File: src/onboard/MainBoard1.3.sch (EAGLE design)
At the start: 82 parts, among them IC1 MIC29310-5.0BT, IC3 A5975D, U1 ADAFRUIT_BMP280_BAROMETER

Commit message: Added gnd test point
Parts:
- added GND: PTR1B1,27, testpad:PTR1B1,27
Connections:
- net GND: now also GND.TP
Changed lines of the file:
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@@
 <part name="C4" library="capacitor-wima" library_urn="urn:adsk.eagle:library:116" deviceset="C" device="2,5-3" package3d_urn="urn:adsk.eagle:package:5436/1" value="10uF"/>
 <part name="SJ1" library="jumper" library_urn="urn:adsk.eagle:library:252" deviceset="SJ" device="" package3d_urn="urn:adsk.eagle:package:15471/1"/>
+<part name="GND" library="testpad" library_urn="urn:adsk.eagle:library:385" deviceset="PTR1" device="B1,27" package3d_urn="urn:adsk.eagle:package:27944/2"/>
 </parts>
 <sheets>
@@
 <attribute name="TP_SIGNAL_NAME" x="10.16" y="69.85" size="1.778" layer="97" rot="R270"/>
 </instance>
+<instance part="GND" gate="G$1" x="12.7" y="45.72" smashed="yes" rot="R270">
+<attribute name="NAME" x="6.35" y="46.736" size="1.778" layer="95"/>
+<attribute name="TP_SIGNAL_NAME" x="10.16" y="44.45" size="1.778" layer="97" rot="R270"/>
+</instance>
 </instances>
 <busses>
@@
 </segment>
 </net>
+<net name="GND" class="0">
+<segment>
+<pinref part="GND" gate="G$1" pin="TP"/>
+<wire x1="15.24" y1="45.72" x2="17.78" y2="45.72" width="0.1524" layer="91"/>
+<label x="17.78" y="45.72" size="1.778" layer="95"/>
+</segment>
+</net>

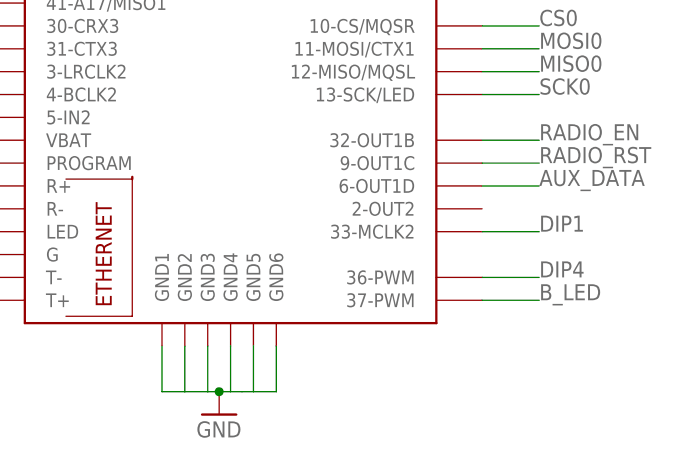
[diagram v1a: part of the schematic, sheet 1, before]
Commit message: Performed ERC and made changes
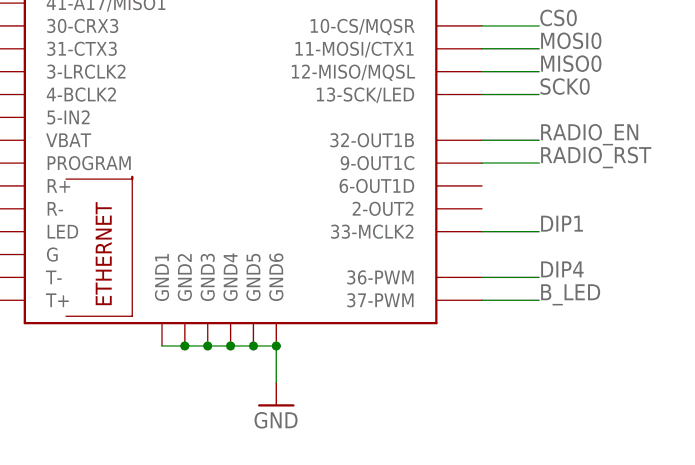
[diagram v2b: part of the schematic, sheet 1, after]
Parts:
- 22V_PWR: value (none) -> 22V_PWR
- 5V_PWR: value (none) -> 5V_PWR
- 6V_PWR: value (none) -> 6V_PWR
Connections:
- removed net AUX_DATA: TEENSY4.1.6-OUT1D
- removed net N$4: AUX.2
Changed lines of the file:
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@@
 <part name="DIPBANK" library="pinhead" library_urn="urn:adsk.eagle:library:325" deviceset="PINHD-1X5" device="" package3d_urn="urn:adsk.eagle:package:22469/2"/>
 <part name="GND11" library="supply1" library_urn="urn:adsk.eagle:library:371" deviceset="GND" device=""/>
-<part name="6V_PWR" library="pinhead" library_urn="urn:adsk.eagle:library:325" deviceset="PINHD-1X3" device="" package3d_urn="urn:adsk.eagle:package:22458/2"/>
+<part name="6V_PWR" library="pinhead" library_urn="urn:adsk.eagle:library:325" deviceset="PINHD-1X3" device="" package3d_urn="urn:adsk.eagle:package:22458/2" value="6V_PWR"/>
 <part name="LEDBANK" library="pinhead" library_urn="urn:adsk.eagle:library:325" deviceset="PINHD-1X7" device="" package3d_urn="urn:adsk.eagle:package:22477/2"/>
 <part name="GND13" library="supply1" library_urn="urn:adsk.eagle:library:371" deviceset="GND" device=""/>
-<part name="22V_PWR" library="pinhead" library_urn="urn:adsk.eagle:library:325" deviceset="PINHD-1X3" device="" package3d_urn="urn:adsk.eagle:package:22458/2"/>
+<part name="22V_PWR" library="pinhead" library_urn="urn:adsk.eagle:library:325" deviceset="PINHD-1X3" device="" package3d_urn="urn:adsk.eagle:package:22458/2" value="22V_PWR"/>
 <part name="GND14" library="supply1" library_urn="urn:adsk.eagle:library:371" deviceset="GND" device=""/>
 <part name="5V" library="testpad" library_urn="urn:adsk.eagle:library:385" deviceset="PTR1" device="B1,27" package3d_urn="urn:adsk.eagle:package:27944/2"/>
@@
 <part name="6V" library="testpad" library_urn="urn:adsk.eagle:library:385" deviceset="PTR1" device="B1,27" package3d_urn="urn:adsk.eagle:package:27944/2"/>
 <part name="GND7" library="supply1" library_urn="urn:adsk.eagle:library:371" deviceset="GND" device=""/>
-<part name="5V_PWR" library="pinhead" library_urn="urn:adsk.eagle:library:325" deviceset="PINHD-1X3" device="" package3d_urn="urn:adsk.eagle:package:22458/2"/>
+<part name="5V_PWR" library="pinhead" library_urn="urn:adsk.eagle:library:325" deviceset="PINHD-1X3" device="" package3d_urn="urn:adsk.eagle:package:22458/2" value="5V_PWR"/>
 <part name="IC1" library="linear" library_urn="urn:adsk.eagle:library:262" deviceset="78*" device="TV" package3d_urn="urn:adsk.eagle:package:16417/2" technology="6" value="MIC29310-5.0BT"/>
 <part name="GND8" library="supply1" library_urn="urn:adsk.eagle:library:371" deviceset="GND" device=""/>
@@
 <instances>
 <instance part="TEENSY4.1" gate="G$1" x="62.23" y="43.18" smashed="yes"/>
-<instance part="GND10" gate="1" x="60.96" y="-7.62" smashed="yes">
-<attribute name="VALUE" x="58.42" y="-10.16" size="1.778" layer="96"/>
+<instance part="GND10" gate="1" x="67.31" y="-6.604" smashed="yes">
+<attribute name="VALUE" x="64.77" y="-9.144" size="1.778" layer="96"/>
 </instance>
 </instances>
@@
 </segment>
 </net>
-<net name="GND" class="0">
-<segment>
-<pinref part="TEENSY4.1" gate="G$1" pin="GND1"/>
-<wire x1="54.61" y1="-5.08" x2="57.15" y2="-5.08" width="0.1524" layer="91"/>
-<wire x1="54.61" y1="0" x2="54.61" y2="-5.08" width="0.1524" layer="91"/>
-<pinref part="TEENSY4.1" gate="G$1" pin="GND3"/>
-<wire x1="59.69" y1="0" x2="59.69" y2="-5.08" width="0.1524" layer="91"/>
-<pinref part="TEENSY4.1" gate="G$1" pin="GND6"/>
-<wire x1="67.31" y1="0" x2="67.31" y2="-5.08" width="0.1524" layer="91"/>
-<wire x1="67.31" y1="-5.08" x2="64.77" y2="-5.08" width="0.1524" layer="91"/>
-<pinref part="TEENSY4.1" gate="G$1" pin="GND2"/>
-<wire x1="62.23" y1="-5.08" x2="60.96" y2="-5.08" width="0.1524" layer="91"/>
-<wire x1="60.96" y1="-5.08" x2="59.69" y2="-5.08" width="0.1524" layer="91"/>
-<wire x1="57.15" y1="0" x2="57.15" y2="-5.08" width="0.1524" layer="91"/>
-<wire x1="57.15" y1="-5.08" x2="59.69" y2="-5.08" width="0.1524" layer="91"/>
-<pinref part="TEENSY4.1" gate="G$1" pin="GND4"/>
-<wire x1="62.23" y1="0" x2="62.23" y2="-5.08" width="0.1524" layer="91"/>
-<wire x1="62.23" y1="-5.08" x2="63.5" y2="-5.08" width="0.1524" layer="91"/>
-<pinref part="TEENSY4.1" gate="G$1" pin="GND5"/>
-<wire x1="64.77" y1="0" x2="64.77" y2="-5.08" width="0.1524" layer="91"/>
-<wire x1="64.77" y1="-5.08" x2="63.5" y2="-5.08" width="0.1524" layer="91"/>
-<pinref part="GND10" gate="1" pin="GND"/>
-<junction x="60.96" y="-5.08"/>
-</segment>
-</net>
 <net name="GPS_EN" class="0">
 <segment>
@@
 </segment>
 </net>
-<net name="AUX_DATA" class="0">
-<segment>
-<pinref part="TEENSY4.1" gate="G$1" pin="6-OUT1D"/>
-<wire x1="90.17" y1="17.78" x2="96.52" y2="17.78" width="0.1524" layer="91"/>
-<label x="96.52" y="17.78" size="1.778" layer="95"/>
-</segment>
-</net>
 <net name="BTN2" class="0">
 <segment>
@@
 <wire x1="34.29" y1="45.72" x2="33.02" y2="45.72" width="0.1524" layer="91"/>
 <label x="25.4" y="45.72" size="1.778" layer="95"/>
+</segment>
+</net>
+<net name="GND" class="0">
+<segment>
+<pinref part="TEENSY4.1" gate="G$1" pin="GND1"/>
+<pinref part="TEENSY4.1" gate="G$1" pin="GND2"/>
+<wire x1="54.61" y1="0" x2="57.15" y2="0" width="0.1524" layer="91"/>
+<pinref part="TEENSY4.1" gate="G$1" pin="GND3"/>
+<wire x1="57.15" y1="0" x2="59.69" y2="0" width="0.1524" layer="91"/>
+<junction x="57.15" y="0"/>
+<pinref part="TEENSY4.1" gate="G$1" pin="GND4"/>
+<wire x1="59.69" y1="0" x2="62.23" y2="0" width="0.1524" layer="91"/>
+<junction x="59.69" y="0"/>
+<pinref part="TEENSY4.1" gate="G$1" pin="GND5"/>
+<wire x1="62.23" y1="0" x2="64.77" y2="0" width="0.1524" layer="91"/>
+<junction x="62.23" y="0"/>
+<pinref part="TEENSY4.1" gate="G$1" pin="GND6"/>
+<wire x1="64.77" y1="0" x2="67.31" y2="0" width="0.1524" layer="91"/>
+<junction x="64.77" y="0"/>
+<pinref part="GND10" gate="1" pin="GND"/>
+<wire x1="67.31" y1="0" x2="67.31" y2="-4.064" width="0.1524" layer="91"/>
+<junction x="67.31" y="0"/>
 </segment>
 </net>
@@
 <net name="PWM13" class="0">
 <segment>
-<pinref part="R13" gate="G$1" pin="1"/>
-<wire x1="25.4" y1="27.94" x2="22.86" y2="27.94" width="0.1524" layer="91"/>
-</segment>
-<segment>
 <pinref part="SERVO_DRIVER" gate="G$1" pin="LED13"/>
 <wire x1="86.36" y1="109.22" x2="91.44" y2="109.22" width="0.1524" layer="91"/>
@@
 </segment>
 <segment>
+<pinref part="R13" gate="G$1" pin="1"/>
+<wire x1="25.4" y1="27.94" x2="22.86" y2="27.94" width="0.1524" layer="91"/>
 <label x="22.86" y="27.94" size="1.778" layer="95" align="bottom-right"/>
 </segment>
 </net>
 <net name="PWM12" class="0">
-<segment>
-<pinref part="R14" gate="G$1" pin="1"/>
-<wire x1="25.4" y1="10.16" x2="22.86" y2="10.16" width="0.1524" layer="91"/>
-</segment>
 <segment>
 <pinref part="SERVO_DRIVER" gate="G$1" pin="LED12"/>
@@
 </segment>
 <segment>
+<pinref part="R14" gate="G$1" pin="1"/>
+<wire x1="25.4" y1="10.16" x2="22.86" y2="10.16" width="0.1524" layer="91"/>
 <label x="22.86" y="10.16" size="1.778" layer="95" align="bottom-right"/>
 </segment>
@@
 <instance part="6V_PWR" gate="A" x="-7.62" y="78.74" smashed="yes" rot="R90">
 <attribute name="NAME" x="-7.239" y="81.28" size="1.778" layer="95" align="center"/>
-<attribute name="VALUE" x="0" y="72.39" size="1.778" layer="96" rot="R90"/>
 </instance>
 <instance part="22V_PWR" gate="A" x="10.16" y="78.74" smashed="yes" rot="R90">
 <attribute name="NAME" x="10.541" y="81.28" size="1.778" layer="95" align="center"/>
-<attribute name="VALUE" x="17.78" y="72.39" size="1.778" layer="96" rot="R90"/>
 </instance>
 <instance part="GND14" gate="1" x="12.7" y="68.58" smashed="yes">
@@
 <instance part="5V_PWR" gate="A" x="-25.4" y="78.74" smashed="yes" rot="R90">
 <attribute name="NAME" x="-25.019" y="81.28" size="1.778" layer="95" align="center"/>
-<attribute name="VALUE" x="-17.78" y="72.39" size="1.778" layer="96" rot="R90"/>
 </instance>
 <instance part="IC1" gate="A1" x="20.32" y="-20.32" smashed="yes">
@@
 </segment>
 </net>
-<net name="N$4" class="0">
-<segment>
-<pinref part="AUX" gate="A" pin="2"/>
-<wire x1="73.66" y1="60.96" x2="81.28" y2="60.96" width="0.1524" layer="91"/>
-</segment>
-</net>
 <net name="AUX" class="0">
 <segment>
@@
 </sheet>
 </sheets>
+<errors>
+</errors>
 </schematic>
 </drawing>

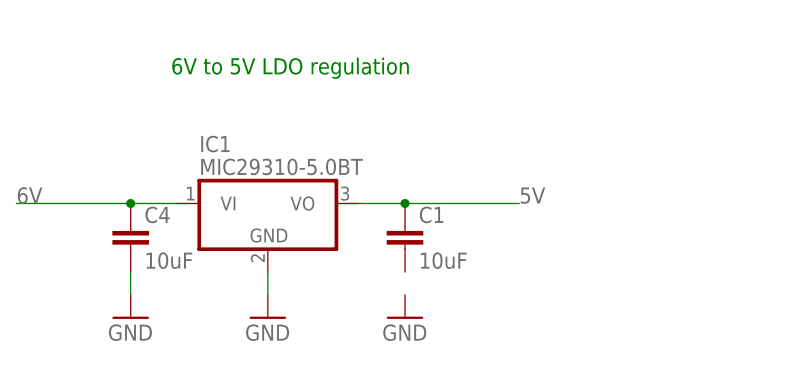
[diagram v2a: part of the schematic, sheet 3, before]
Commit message: Updated BMP 280 VIN pin to be IO
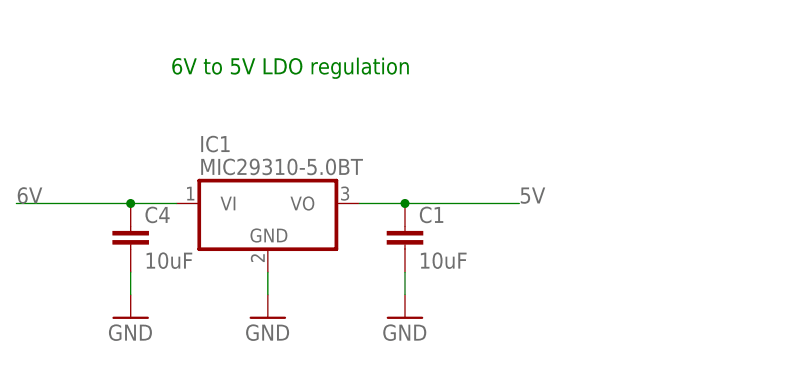
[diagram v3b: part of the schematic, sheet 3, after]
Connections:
- net GND: now also C1.2
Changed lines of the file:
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@@
 <wire x1="5.08" y1="-27.94" x2="5.08" y2="-30.48" width="0.1524" layer="91"/>
+</segment>
+<segment>
+<pinref part="C1" gate="G$1" pin="2"/>
+<pinref part="GND18" gate="1" pin="GND"/>
+<wire x1="35.56" y1="-27.94" x2="35.56" y2="-30.48" width="0.1524" layer="91"/>
 </segment>
 </net>

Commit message: Update for TBS Unify FPV transmitter
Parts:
- removed R10, R11, R12, R13, R14, R15, R16, R17: 220, adafruit:R-US_0204/7
- removed SV10, SV11, SV12, SV13, SV14, SV15, SV9: (no value), con-lstb:MA03-1
- removed U1: ADAFRUIT_BMP280_BAROMETER, AERO_Eagle_Library:ADAFRUIT_BMP280_BAROMETER
- added FPV: (no value), con-lstb:MA03-1
- added IC2: ADAFRUIT_BMP280, Adafruit_BMP280:ADAFRUIT_BMP280
- SV8: device con-lstb:MA03-1 -> con-lstb:MA05-1
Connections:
- removed net N$109: R12.2, SV9.1
- removed net N$112: R16.2, SV15.1
- removed net N$115: R17.2, SV14.1
- removed net N$118: R13.2, SV13.1
- removed net N$2: R14.2, SV12.1
- removed net N$43: R10.2, SV11.1
- removed net N$91: R11.2, SV10.1
- removed net N$94: R15.2, SV8.1
- removed net PWM10: R11.1, SERVO_DRIVER.LED10
- removed net PWM11: R10.1, SERVO_DRIVER.LED11
- removed net PWM12: R14.1, SERVO_DRIVER.LED12
- removed net PWM13: R13.1, SERVO_DRIVER.LED13
- removed net PWM14: R17.1, SERVO_DRIVER.LED14
- removed net PWM15: R16.1, SERVO_DRIVER.LED15
- removed net PWM8: R15.1, SERVO_DRIVER.LED8
- removed net PWM9: R12.1, SERVO_DRIVER.LED9
- new net VIDEO: FPV.3, SV8.5
- net 5V: now also FPV.1, IC2.VIN, SV8.1, SV8.3; no longer SV10.2, SV11.2, SV12.2, SV13.2, SV14.2, SV15.2, SV8.2, SV9.2, U1.VIN
- net GND: now also FPV.2, IC2.GND, SV8.2, SV8.4; no longer SV10.3, SV11.3, SV12.3, SV13.3, SV14.3, SV15.3, SV8.3, SV9.3, U1.GND
- net SCL: now also IC2.SCK; no longer U1.SCK
- net SDA: now also IC2.SDI; no longer U1.SDI

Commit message: AKK iteration (incomplete)
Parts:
- removed FPV: (no value), con-lstb:MA03-1
- removed SV8: (no value), con-lstb:MA05-1
- added JP1: (no value), pinhead:PINHD-1X2
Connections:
- removed net VIDEO: FPV.3, SV8.5
- net 5V: now also JP1.1; no longer FPV.1, SV8.1, SV8.3
- net GND: now also JP1.2; no longer FPV.2, SV8.2, SV8.4
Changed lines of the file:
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@@
 <part name="GND" library="testpad" library_urn="urn:adsk.eagle:library:385" deviceset="PTR1" device="B1,27" package3d_urn="urn:adsk.eagle:package:27944/2"/>
 <part name="IC2" library="Adafruit_BMP280" deviceset="ADAFRUIT_BMP280" device=""/>
-<part name="FPV" library="con-lstb" library_urn="urn:adsk.eagle:library:162" deviceset="MA03-1" device="" package3d_urn="urn:adsk.eagle:package:8339/1"/>
-<part name="SV8" library="con-lstb" library_urn="urn:adsk.eagle:library:162" deviceset="MA05-1" device="" package3d_urn="urn:adsk.eagle:package:8332/1"/>
+<part name="JP1" library="pinhead" library_urn="urn:adsk.eagle:library:325" deviceset="PINHD-1X2" device="" package3d_urn="urn:adsk.eagle:package:22435/2"/>
 </parts>
 <sheets>
@@
 <attribute name="VALUE" x="21.59" y="20.32" size="1.778" layer="96" align="center-left"/>
 </instance>
-<instance part="FPV" gate="G$1" x="104.14" y="5.08" smashed="yes">
-<attribute name="VALUE" x="102.87" y="-2.54" size="1.778" layer="96"/>
-<attribute name="NAME" x="102.87" y="10.922" size="1.778" layer="95"/>
-</instance>
-<instance part="SV8" gate="G$1" x="129.54" y="5.08" smashed="yes">
-<attribute name="VALUE" x="128.27" y="-5.08" size="1.778" layer="96"/>
-<attribute name="NAME" x="128.27" y="13.462" size="1.778" layer="95"/>
+<instance part="JP1" gate="G$1" x="139.7" y="5.08" smashed="yes">
+<attribute name="NAME" x="133.35" y="10.795" size="1.778" layer="95"/>
+<attribute name="VALUE" x="133.35" y="0" size="1.778" layer="96"/>
 </instance>
 </instances>
@@
 </segment>
 <segment>
-<pinref part="SV8" gate="G$1" pin="3"/>
-<wire x1="137.16" y1="5.08" x2="142.24" y2="5.08" width="0.1524" layer="91"/>
-<label x="142.24" y="5.08" size="1.778" layer="95"/>
-</segment>
-<segment>
-<pinref part="SV8" gate="G$1" pin="1"/>
-<wire x1="137.16" y1="0" x2="142.24" y2="0" width="0.1524" layer="91"/>
-<label x="142.24" y="0" size="1.778" layer="95"/>
-</segment>
-<segment>
-<pinref part="FPV" gate="G$1" pin="1"/>
-<wire x1="111.76" y1="2.54" x2="114.3" y2="2.54" width="0.1524" layer="91"/>
-<label x="114.3" y="2.54" size="1.778" layer="95"/>
+<pinref part="JP1" gate="G$1" pin="1"/>
+<wire x1="137.16" y1="7.62" x2="129.54" y2="7.62" width="0.1524" layer="91"/>
+<label x="129.54" y="7.62" size="1.778" layer="95"/>
 </segment>
 </net>
@@
 </segment>
 <segment>
-<pinref part="SV8" gate="G$1" pin="4"/>
-<wire x1="137.16" y1="7.62" x2="142.24" y2="7.62" width="0.1524" layer="91"/>
-<label x="142.24" y="7.62" size="1.778" layer="95"/>
-</segment>
-<segment>
-<pinref part="SV8" gate="G$1" pin="2"/>
-<wire x1="137.16" y1="2.54" x2="142.24" y2="2.54" width="0.1524" layer="91"/>
-<label x="142.24" y="2.54" size="1.778" layer="95"/>
-</segment>
-<segment>
-<pinref part="FPV" gate="G$1" pin="2"/>
-<wire x1="111.76" y1="5.08" x2="114.3" y2="5.08" width="0.1524" layer="91"/>
-<label x="114.3" y="5.08" size="1.778" layer="95"/>
+<pinref part="JP1" gate="G$1" pin="2"/>
+<wire x1="137.16" y1="5.08" x2="129.54" y2="5.08" width="0.1524" layer="91"/>
+<label x="129.54" y="5.08" size="1.778" layer="95"/>
 </segment>
 </net>
@@
 </segment>
 </net>
-<net name="VIDEO" class="0">
-<segment>
-<pinref part="SV8" gate="G$1" pin="5"/>
-<wire x1="137.16" y1="10.16" x2="142.24" y2="10.16" width="0.1524" layer="91"/>
-<label x="142.24" y="10.16" size="1.778" layer="95"/>
-</segment>
-<segment>
-<pinref part="FPV" gate="G$1" pin="3"/>
-<wire x1="111.76" y1="7.62" x2="114.3" y2="7.62" width="0.1524" layer="91"/>
-<label x="114.3" y="7.62" size="1.778" layer="95"/>
-</segment>
-</net>
